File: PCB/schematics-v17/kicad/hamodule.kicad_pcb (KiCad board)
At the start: 2 copper layers, 76.7 x 84.3 mm, 86 parts, among them J1 2604-1104, J10 EspSense, J11 Conn_01x02_Male, J12 NoCon, J2 2604-1102, J3 USB_C_Receptacle_USB2.0, J4 ESP Relays, J5 Current Jumper, J6 GND 3.3V, J7 Conn_01x02, J8 Current Jumper, J9 2604-1104, K1 PCN-105D, K2 PCN-105D, K3 PCN-105D, K4 PCN-105D, Q1 SS8050, Q2 SS8050, SW1 EN, SW2 IO0, U1 ULN2003A, U2 ESP32-WROOM-32E, U4 LD1117AV33_TO220, U5 MCP9700T-ETT, U6 LDA210-PDIP, U7 LDA210-PDIP, U8 CP2102N-A01-GQFN28

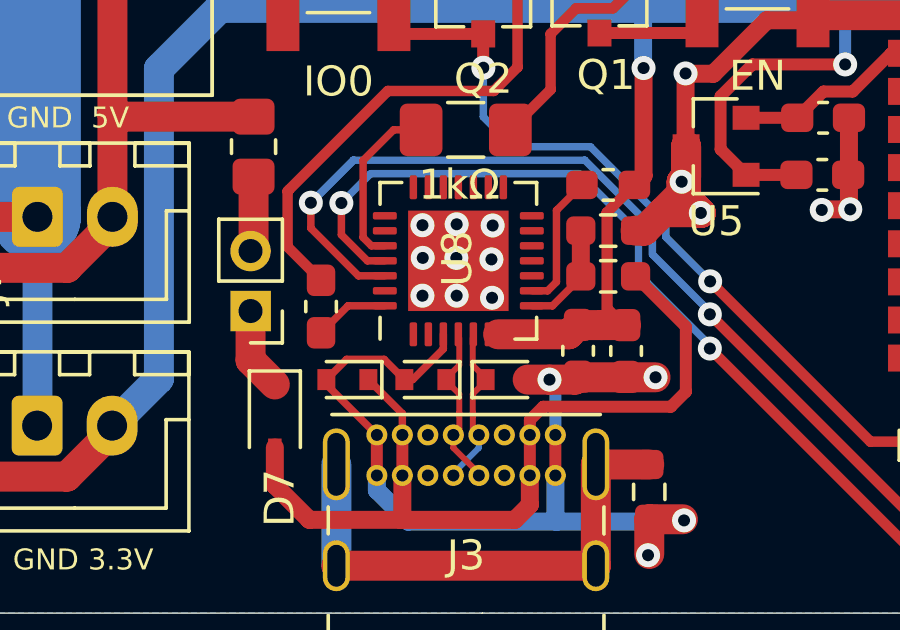
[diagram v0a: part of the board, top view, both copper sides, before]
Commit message: adding usb-c, reduce D+/- lenght, broke d View :(
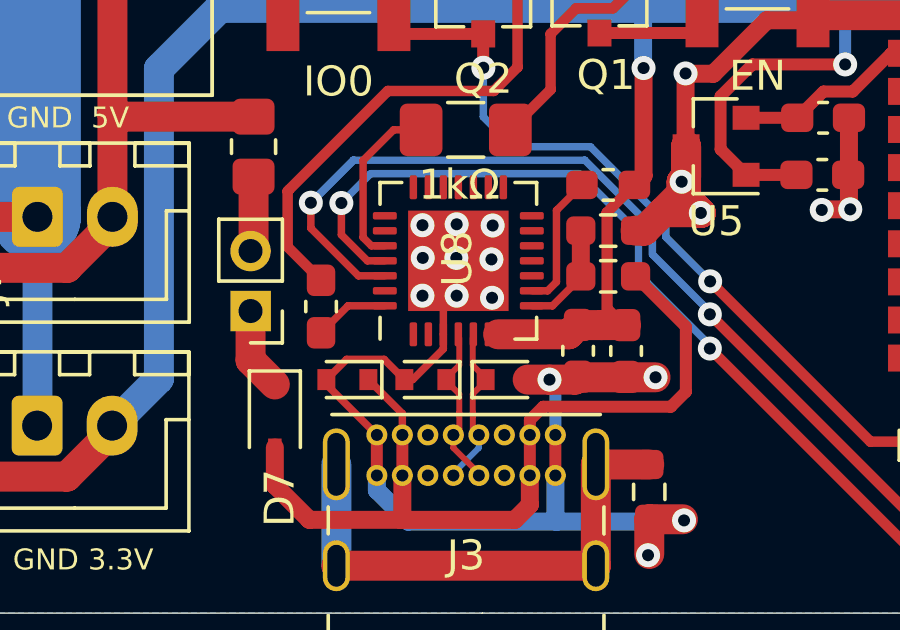
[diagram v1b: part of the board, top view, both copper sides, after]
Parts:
- R12: value 22.1kΩ -> NC
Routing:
- net GND: track 228.1 -> 229.6 mm
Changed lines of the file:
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@@
     (descr "Resistor SMD 0603 (1608 Metric), square (rectangular) end terminal, IPC_7351 nominal with elongated pad for handsoldering. (Body size source: IPC-SM-782 page 72, https://www.pcb-3d.com/wordpress/wp-content/uploads/ipc-sm-782a_amendment_1_and_2.pdf), generated with kicad-footprint-generator")
     (tags "resistor handsolder")
-    (property "JLCPCB" "C25961")
+    (property "JLCPCB" "")
     (property "Sheetfile" "hamodule.kicad_sch")
     (property "Sheetname" "")
@@
       (effects (font (size 1 1) (thickness 0.15)) (justify mirror))
     )
-    (fp_text value "22.1kΩ" (at 0 1.43 90) (layer "B.Fab") hide
+    (fp_text value "NC" (at 0 1.43 90) (layer "B.Fab") hide
       (effects (font (size 1 1) (thickness 0.15)) (justify mirror))
     )
@@
   (segment (start 168.6245 136.1415) (end 168.6245 137.1755) (width 1) (layer "F.Cu") (net 55))
   (segment (start 189.6745 118.6815) (end 189.6745 121.4755) (width 1) (layer "F.Cu") (net 55))
+  (segment (start 160.533 141.5654) (end 160.9765 141.1219) (width 0.25) (layer "F.Cu") (net 55))
   (segment (start 167.6065 143.8419) (end 165.0455 143.8419) (width 1) (layer "F.Cu") (net 55))
   (segment (start 128.869998 138.4935) (end 127.52249 139.841008) (width 1) (layer "F.Cu") (net 55))
@@
   (segment (start 187.946686 126.886314) (end 189.243314 126.886314) (width 0.4) (layer "F.Cu") (net 55))
   (segment (start 168.2115 116.0765) (end 168.9295 116.0765) (width 1) (layer "F.Cu") (net 55))
+  (segment (start 160.533 142.4089) (end 160.533 141.5654) (width 0.25) (layer "F.Cu") (net 55))
   (segment (start 156.94649 114.40149) (end 156.6545 114.1095) (width 1) (layer "F.Cu") (net 55))
   (segment (start 155.1855 127.3745) (end 155.1855 132.0685) (width 1) (layer "F.Cu") (net 55))

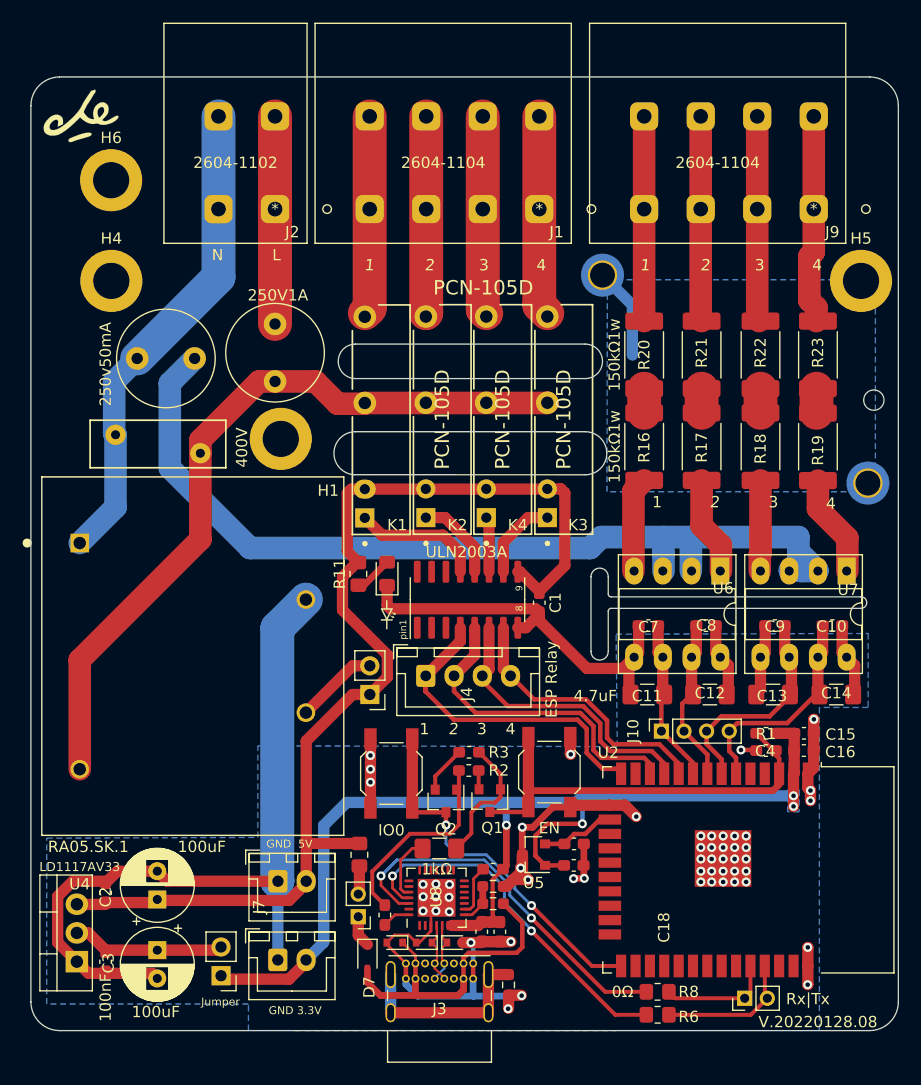
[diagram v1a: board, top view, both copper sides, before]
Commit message: updating libraries to kicad6. some footprints got bigger :S
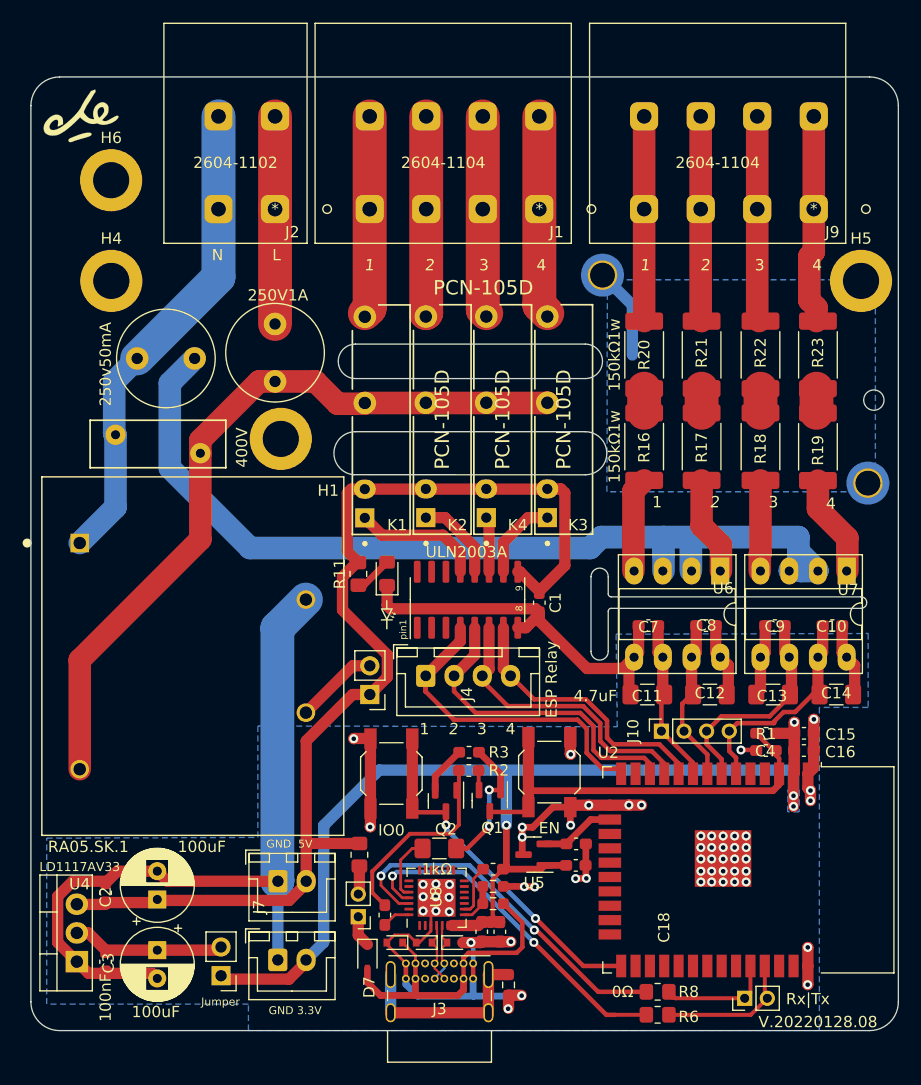
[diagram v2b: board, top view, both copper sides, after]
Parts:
- moved C17 0.18 mm to (173.4, 135.2)
- moved C6 0.18 mm to (173.3, 137.1)
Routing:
- net 3.3V+: track 103.3 -> 109.1 mm
- net Net-(R8-Pad2): track 35.4 -> 32.5 mm
- net GND: track 229.6 -> 226.8 mm, vias 54 -> 57
- net Net-(R6-Pad2): track 32.1 -> 30.7 mm
- net IO0: track 32.3 -> 31.3 mm
- net RTS: track 11.6 -> 12.1 mm, vias 0 -> 2

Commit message: fixing transistor symbol. pinout was wrong :(
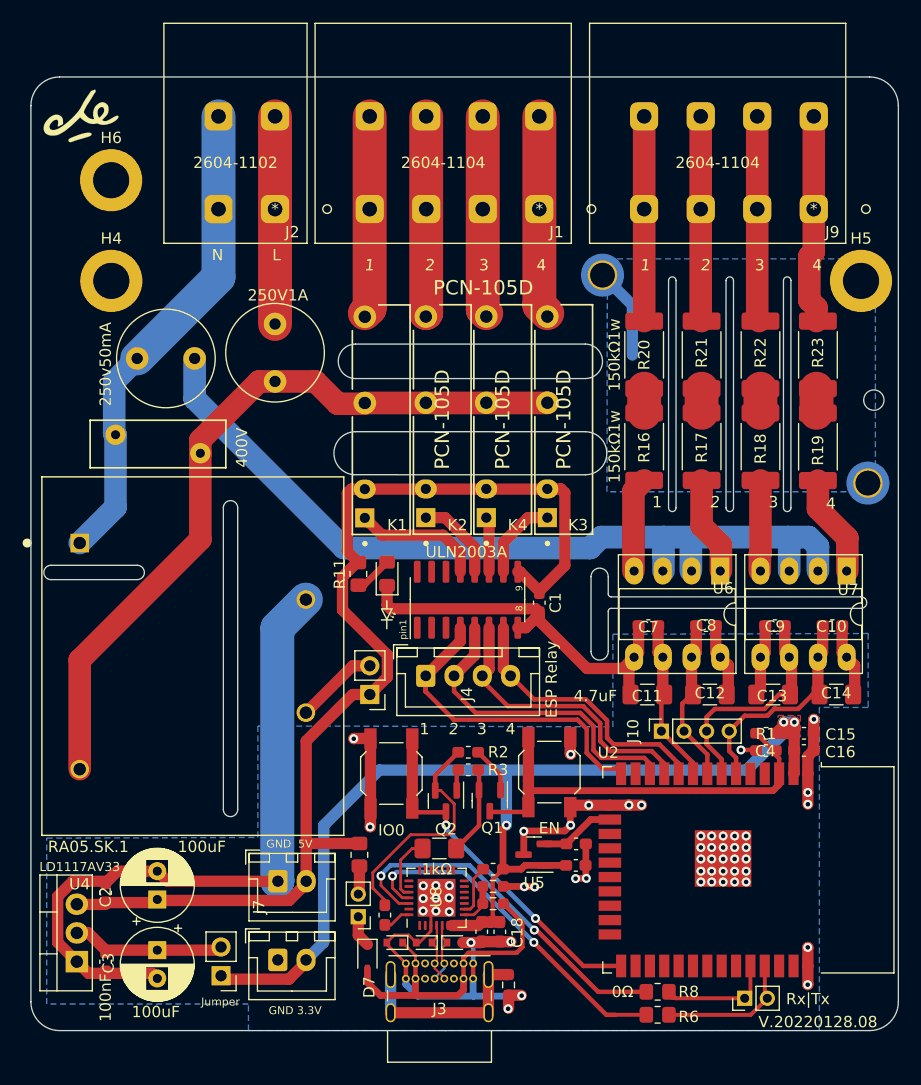
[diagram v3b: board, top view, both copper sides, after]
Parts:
- removed H1: MountingHole_Pad, MountingHole:MountingHole_3.2mm_M3_ISO14580_Pad
- Q1: value SS8050 -> SS8050-SMD
- moved R2 1.61 mm to (163.8, 127.1)
- moved R3 1.55 mm to (163.8, 128.6)
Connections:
- Q1 pad 1: RTS -> Net-(Q1-Pad1)
- Q1 pad 2: Net-(Q1-Pad2) -> RTS
- Q2 pad 1: DTR -> Net-(R3-Pad1)
- Q2 pad 2: Net-(Q2-Pad2) -> DTR
- R2 pad 1: Net-(Q1-Pad2) -> Net-(Q1-Pad1)
- R3 pad 1: Net-(Q2-Pad2) -> Net-(R3-Pad1)
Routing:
- net GND: track 226.8 -> 219.0 mm, vias 57 -> 56
- net 220VAC(N): track 83.6 -> 76.1 mm
- net RTS: track 12.1 -> 7.83 mm, vias 2 -> 0
- net Net-(Q2-Pad2): track 4.25 -> 0.00 mm
- net Net-(Q1-Pad1): track 0.00 -> 4.16 mm
- net Net-(R3-Pad1): track 0.00 -> 1.88 mm
- net Net-(Q1-Pad2): track 1.68 -> 0.00 mm
- net DTR: track 19.1 -> 20.8 mm
- net EspSens3: track 19.2 -> 19.8 mm
- net 3.3V+: track 109.1 -> 109.3 mm, vias 4 -> 3
- added copper zone on F.Cu, net 3.3V+
- removed copper zone on B.Cu, net 3.3V+
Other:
- outline, holes or cut-outs redrawn

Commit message: fixing kicad6 library reference. Using the right transistor package. Fixing 3D for some components
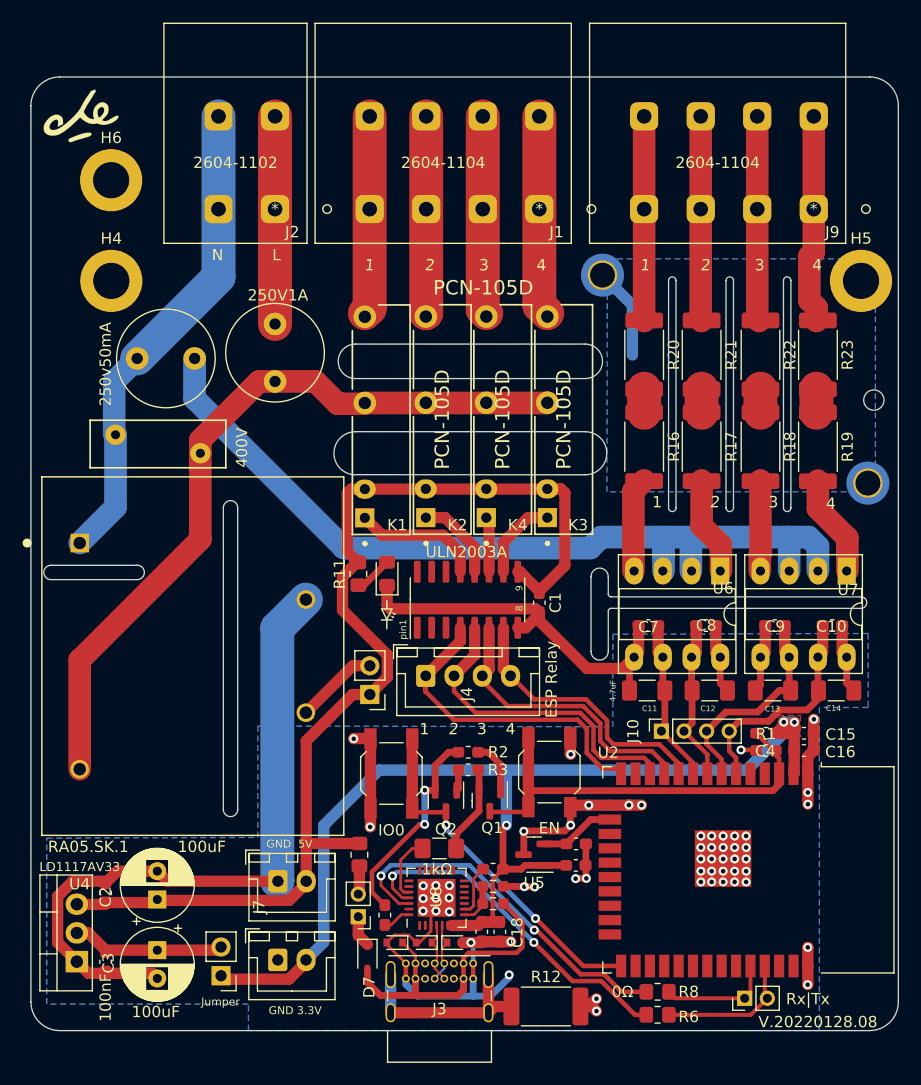
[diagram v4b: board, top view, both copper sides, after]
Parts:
- C11, C12, C13, C14: footprint Capacitor_SMD:C_1206_3216Metric_Pad1.42x1.75mm_HandSolder -> Capacitor_SMD:C_1206_3216Metric_Pad1.33x1.80mm_HandSolder
- R12: value NC -> 150kΩ1w; footprint Resistor_SMD:R_0603_1608Metric_Pad0.98x0.95mm_HandSolder -> Resistor_SMD:R_2512_6332Metric_Pad1.40x3.35mm_HandSolder
- R16, R17, R18, R19, R20, R21, R22, R23: footprint Resistor_SMD:R_2512_6332Metric_Pad1.52x3.35mm_HandSolder -> Resistor_SMD:R_2512_6332Metric_Pad1.40x3.35mm_HandSolder
- moved R12 3.82 mm to (170.7, 149.6), turned to 0 degrees
- moved C13 0.36 mm to (190.8, 121.6)
- moved C14 0.36 mm to (196.4, 121.6)
- moved C11 0.36 mm to (179.7, 121.6)
- moved C12 0.36 mm to (185.2, 121.6)
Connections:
- R12 pad 1: GND -> Net-(J3-PadS1)
- R12 pad 2: Net-(J3-PadS1) -> GND
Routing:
- net DTR: track 20.8 -> 18.5 mm, vias 0 -> 2
- net EspSens1: track 13.8 -> 14.6 mm
- net EspSens3: track 19.8 -> 19.2 mm
- net Net-(Q1-Pad1): track 4.16 -> 4.68 mm
- net GND: track 219.0 -> 218.9 mm, vias 56 -> 57

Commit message: adding gerber + BOM + new images for README
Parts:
- R1, R2, R24, R3, R4: footprint Resistor_SMD:R_0603_1608Metric_Pad1.05x0.95mm_HandSolder -> Resistor_SMD:R_0603_1608Metric_Pad0.98x0.95mm_HandSolder
- R5: footprint Resistor_SMD:R_1206_3216Metric_Pad1.42x1.75mm_HandSolder -> Resistor_SMD:R_1206_3216Metric_Pad1.30x1.75mm_HandSolder
- moved R12 0.69 mm to (171.4, 149.6)
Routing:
- net GND: track 218.9 -> 221.5 mm
- net Net-(J3-PadS1): track 17.7 -> 18.4 mm

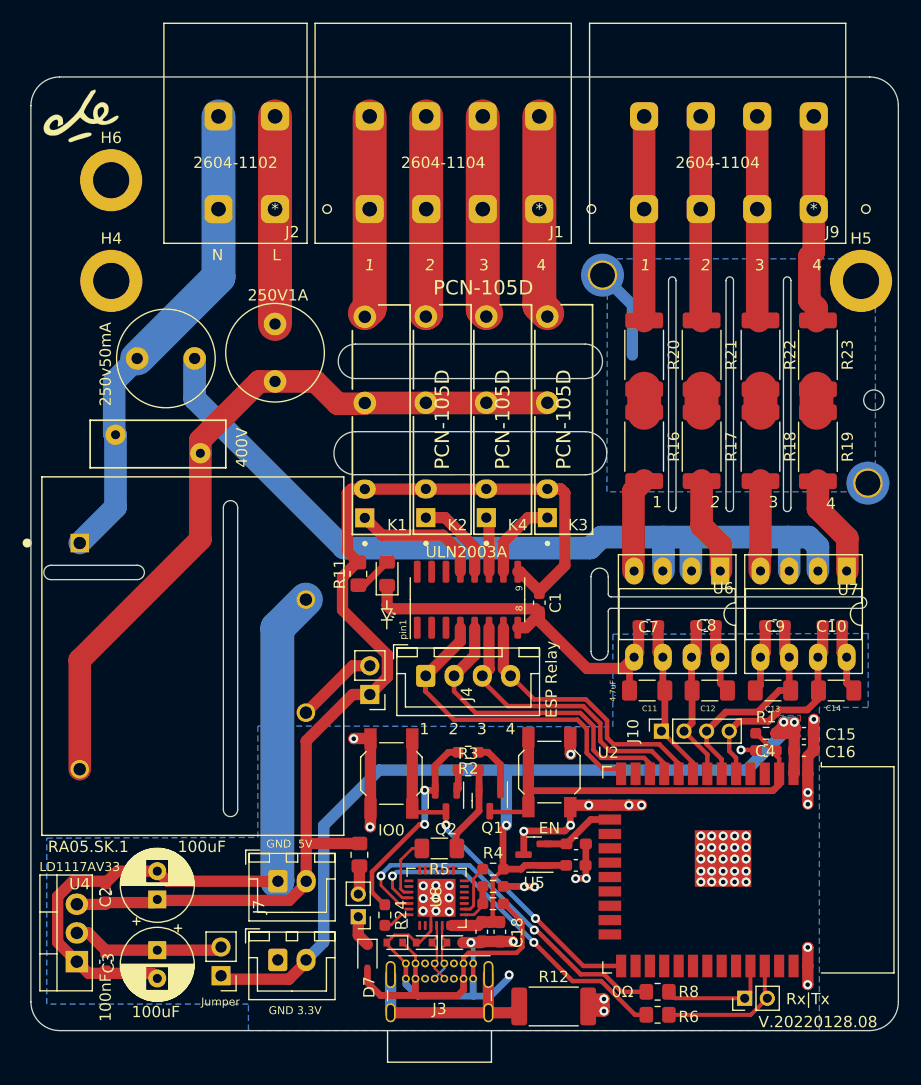
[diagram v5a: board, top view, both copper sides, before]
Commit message: fixing silkscreen + JLCPCB CPL file
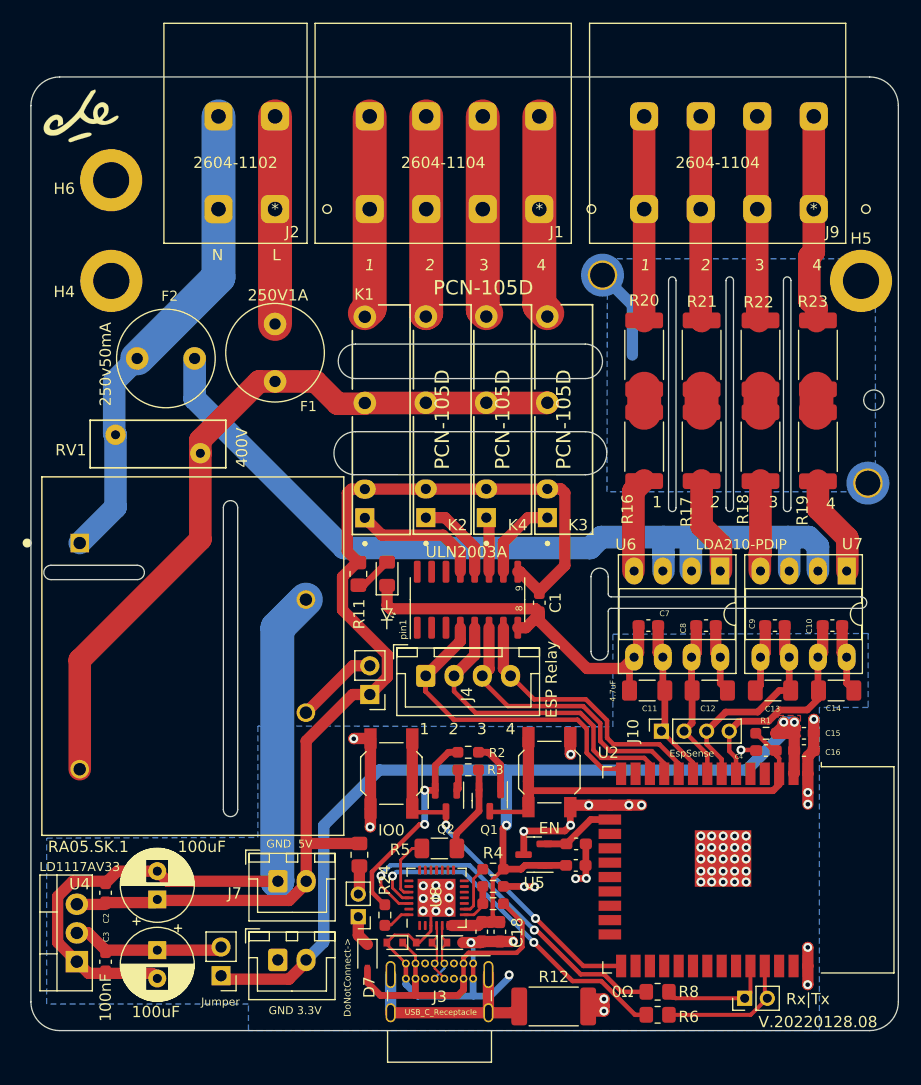
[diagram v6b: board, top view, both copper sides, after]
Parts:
- J12: value NoCon -> DoNotConnect->
- J3: value USB_C_Receptacle_USB2.0 -> USB_C_Receptacle
